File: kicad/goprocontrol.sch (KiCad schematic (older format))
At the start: 23 parts, among them P2 CONN_01X06, Q1 IRLML6344, SW1 Reset, SW2 Prog, U1 LTV-814, U2 ESP-12E, U3 D24V5F3

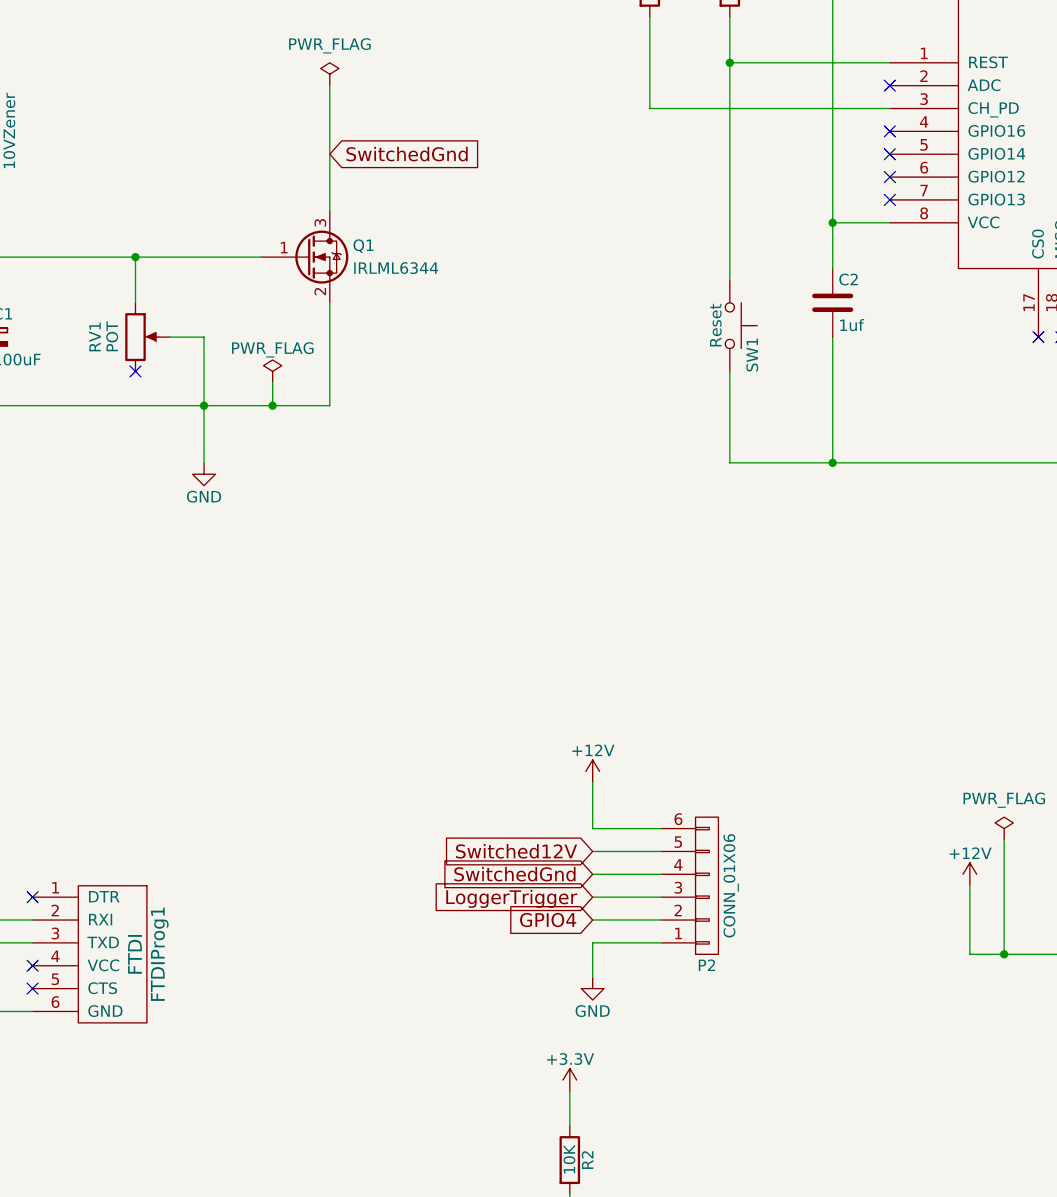
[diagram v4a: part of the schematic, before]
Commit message: v2.5 of the board
- Move main connector to front
- Use MOSFET to drive GPIO12 like MXL2
- Larger traces for Switched Ground
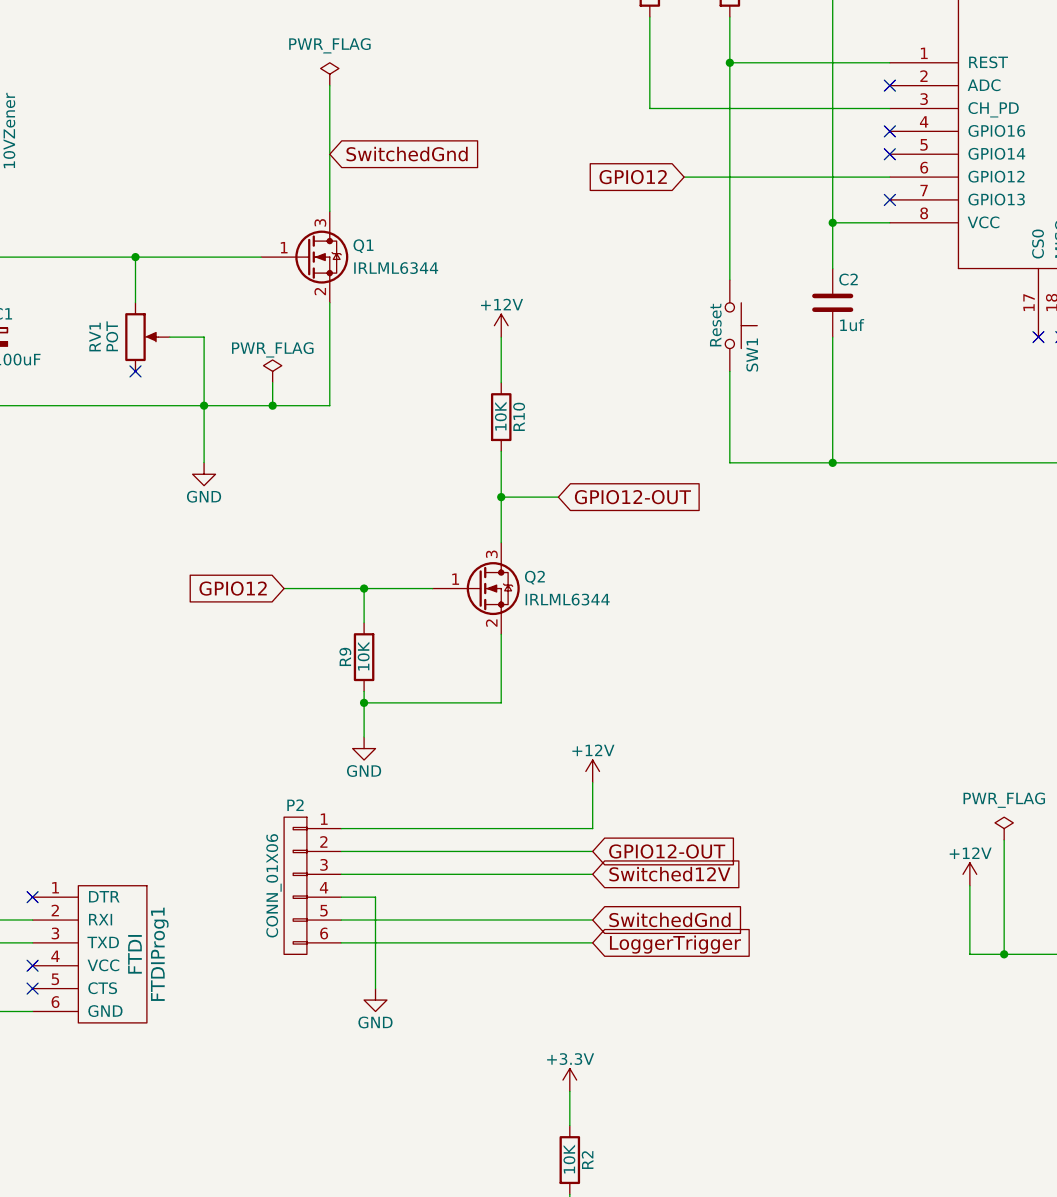
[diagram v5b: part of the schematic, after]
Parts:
- added Q2: IRLML6344, TO_SOT_Packages_SMD:SOT-23_Handsoldering, symbol Q_NMOS_GSD
- added R10, R9: 10K, Resistors_SMD:R_0805_HandSoldering, symbol R
- P2: footprint Connectors_Phoenix:PhoenixContact_MC-G_06x5.08mm_Angled -> Connectors_Phoenix:PhoenixContact_MSTBA-G_06x5.08mm_Angled
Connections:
- net +12V: now also P2.1 (P1), R10.1; no longer P2.6 (P6)
- net GND: now also P2.4 (P4), Q2.2 (S), R9.1; no longer P2.1 (P1)
- net GPIO4: no longer P2.2 (P2)
- net LoggerTrigger: now also P2.6 (P6); no longer P2.3 (P3)
- net Switched12V: now also P2.3 (P3); no longer P2.5 (P5)
- net SwitchedGnd: now also P2.5 (P5); no longer P2.4 (P4)
- net GPIO12: now reaches U2.6 (GPIO12)
- net GPIO12: now also Q2.1 (G), R9.2
- new net GPIO12-OUT: P2.2 (P2), Q2.3 (D), R10.2
- no-connect marks 16 -> 15
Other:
- moved on the sheet: P2
